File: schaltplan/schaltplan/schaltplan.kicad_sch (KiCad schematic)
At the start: 29 parts, among them SW1 Button 1, SW2 Button 2, SW3 Button 3, SW4 Button 4

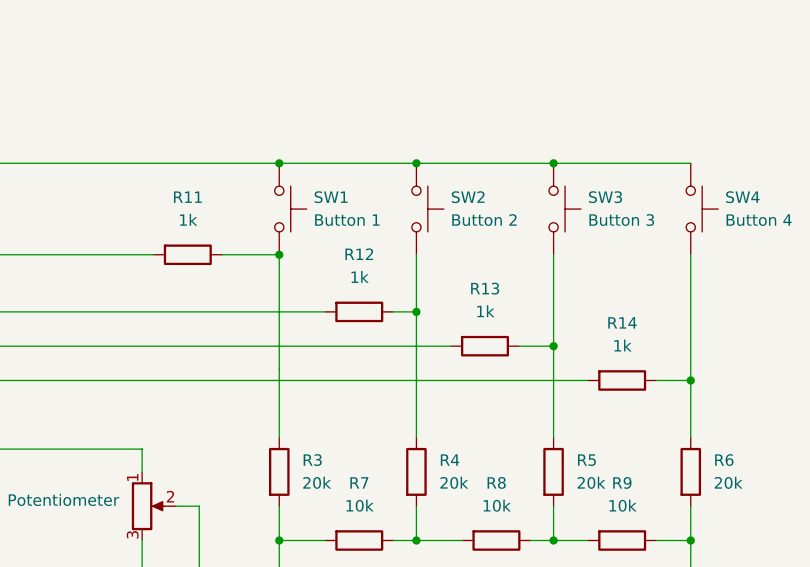
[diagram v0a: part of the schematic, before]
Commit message: schaltplan aktualisiert, hatte die falschen widerstandswerte eingetragen
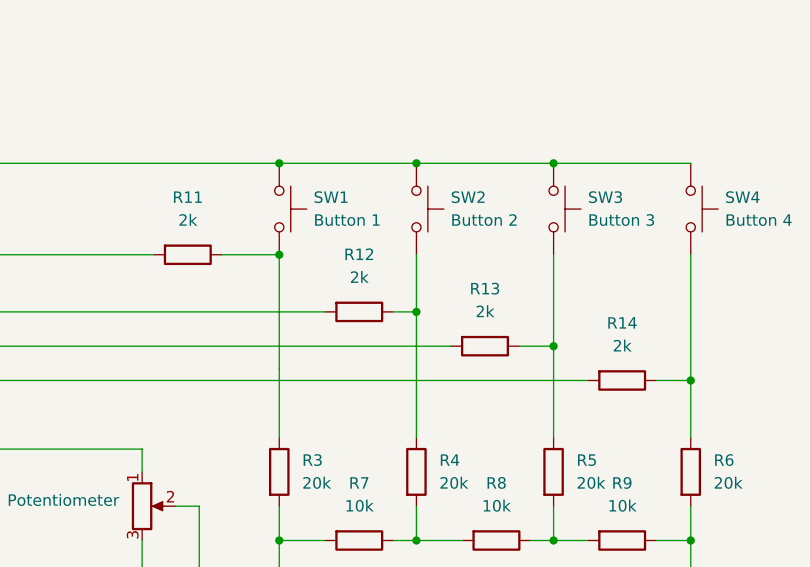
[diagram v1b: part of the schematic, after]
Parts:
- R11, R12, R13, R14: value 1k -> 2k
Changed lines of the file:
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@@
 			)
 		)
-		(property "Value" "1k"
+		(property "Value" "2k"
 			(at 162.56 85.09 90)
 			(effects
@@
 			)
 		)
-		(property "Value" "1k"
+		(property "Value" "2k"
 			(at 176.53 88.9 90)
 			(effects
@@
 			)
 		)
-		(property "Value" "1k"
+		(property "Value" "2k"
 			(at 143.51 78.74 90)
 			(effects
@@
 			)
 		)
-		(property "Value" "1k"
+		(property "Value" "2k"
 			(at 191.77 92.71 90)
 			(effects

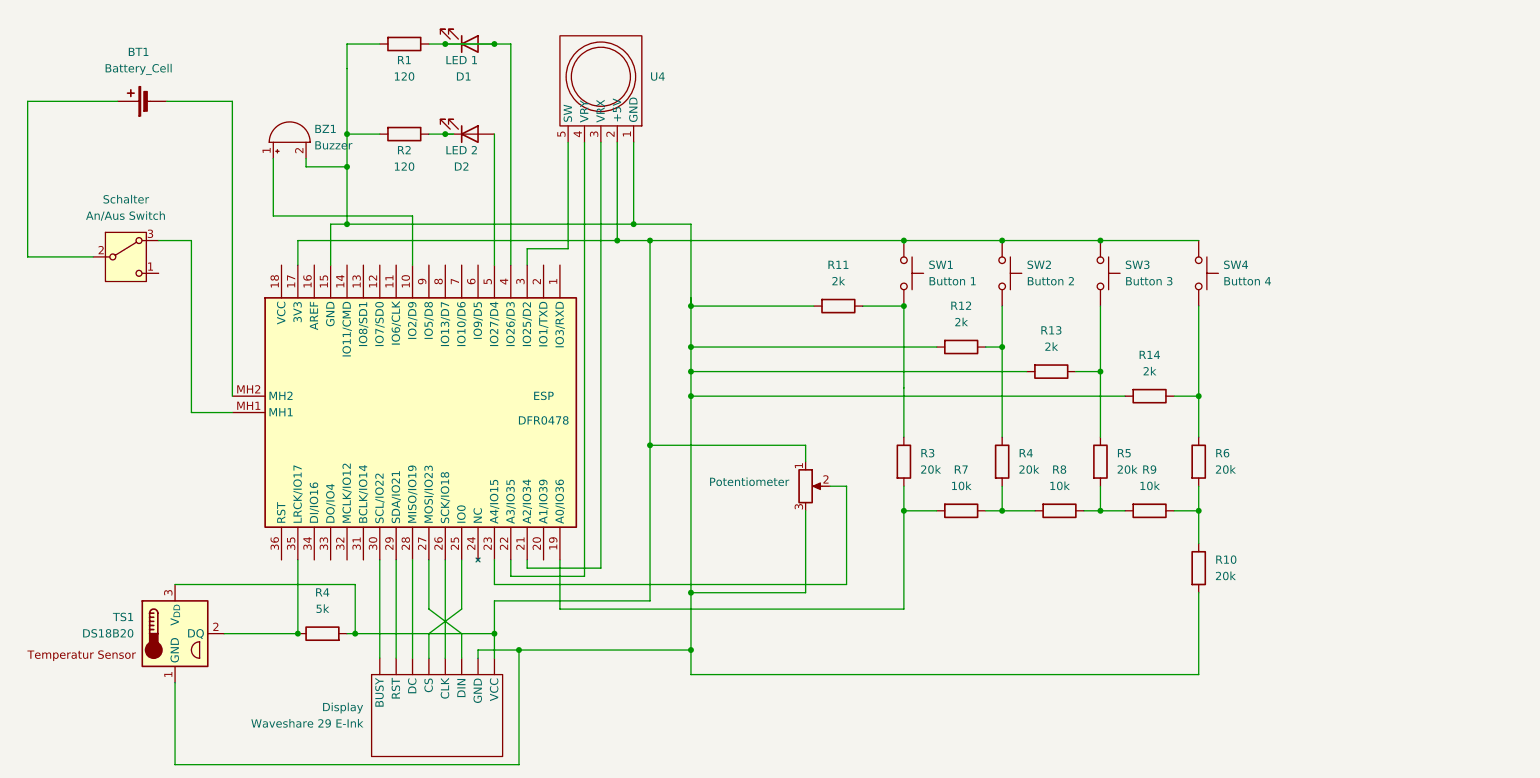
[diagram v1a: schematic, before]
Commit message: Add files via upload
Buzzer im Schaltplan angepasst
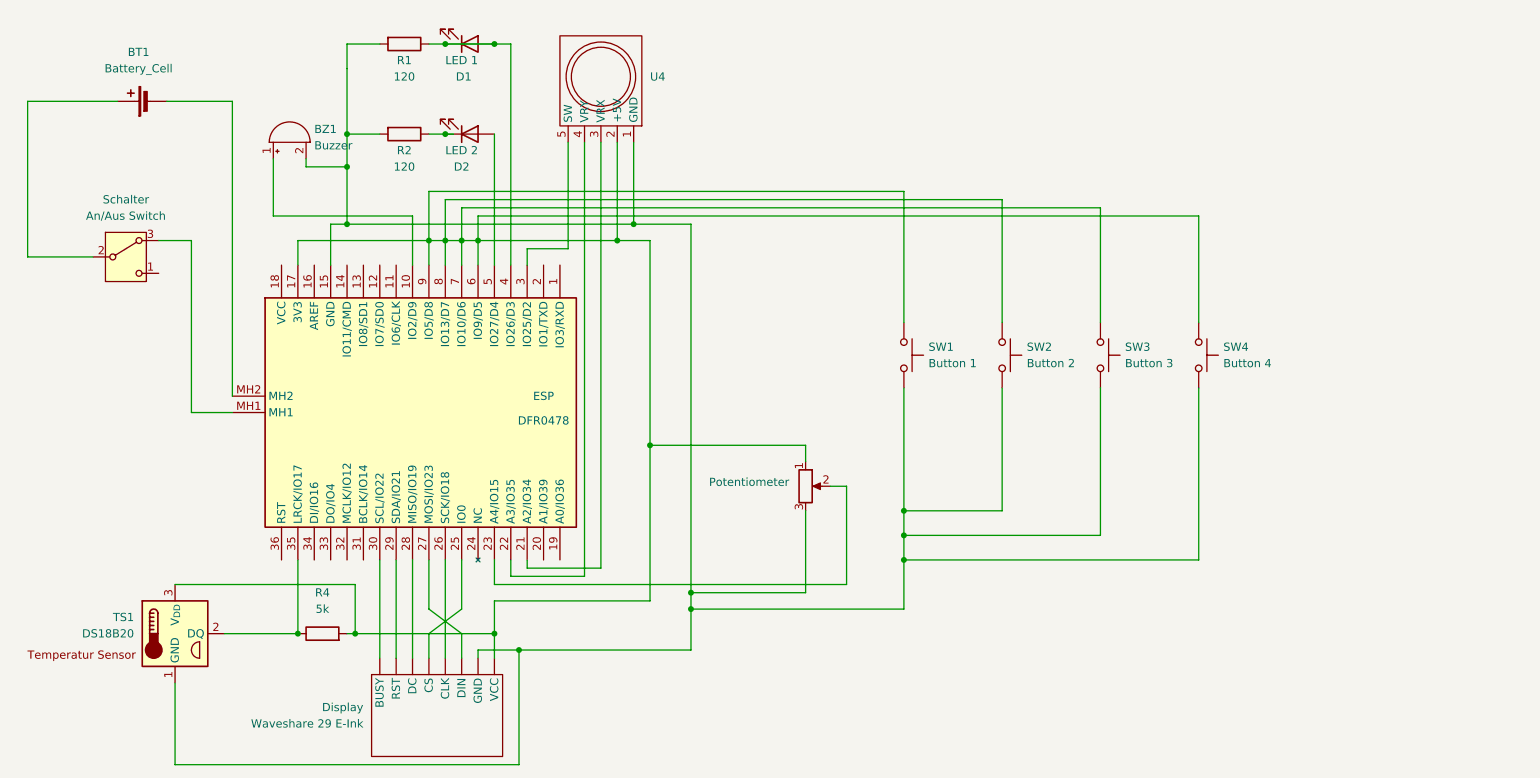
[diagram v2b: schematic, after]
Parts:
- removed R10, R3, R4, R5, R6: 20k, symbol Device:R
- removed R11, R12, R13, R14: 2k, symbol Device:R
- removed R7, R8, R9: 10k, symbol Device:R
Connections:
- net at BZ1.2 (-), Display. (VCC), ESP.15 (GND)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: now also SW1.2, SW2.2, SW3.2, SW4.2
- net at Display. (VCC), ESP.17 (3V3), Potentiometer.1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: now also ESP.6 (IO9/D5), ESP.7 (IO10/D6), ESP.8 (IO13/D7), ESP.9 (IO5/D8)
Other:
- moved on the sheet: SW1, SW2, SW3, SW4

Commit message: schaltplan korrigiert
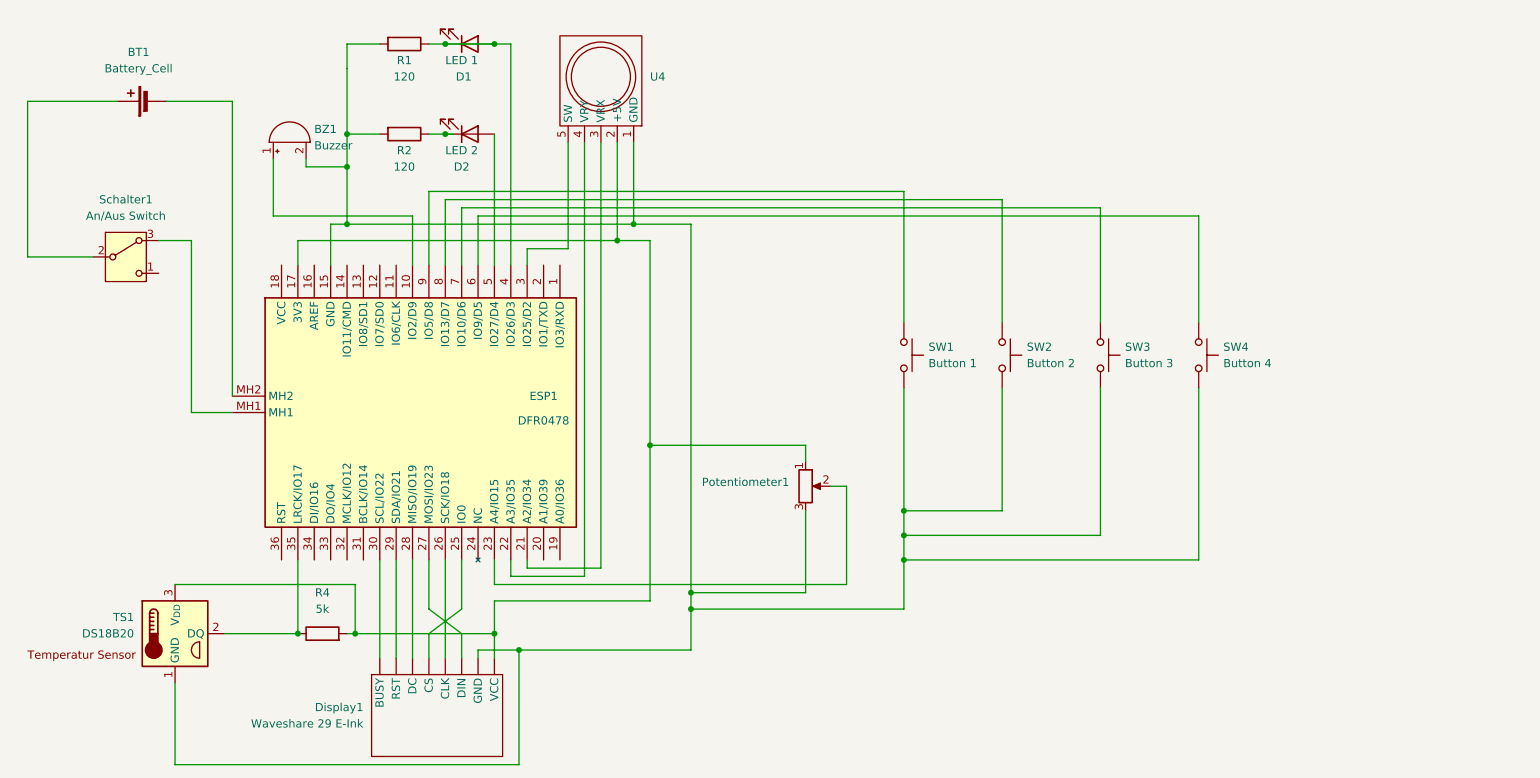
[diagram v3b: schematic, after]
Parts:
- renumbered Display to Display1, ESP to ESP1, Potentiometer to Potentiometer1, Schalter to Schalter1
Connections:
- new net: ESP1.7 (IO10/D6), SW3.1
- new net: ESP1.8 (IO13/D7), SW2.1
- new net: ESP1.9 (IO5/D8), SW1.1
- new net: Display1. (VCC), ESP1.17 (3V3), Potentiometer1.1, R4.2, TS1.3 (V_{DD}), U4.2 (+5V)
- new net: ESP1.6 (IO9/D5), SW4.1

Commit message: spannungsteiler zum schaltplan hinzugefügt und für messung an analog pin angeschlossen
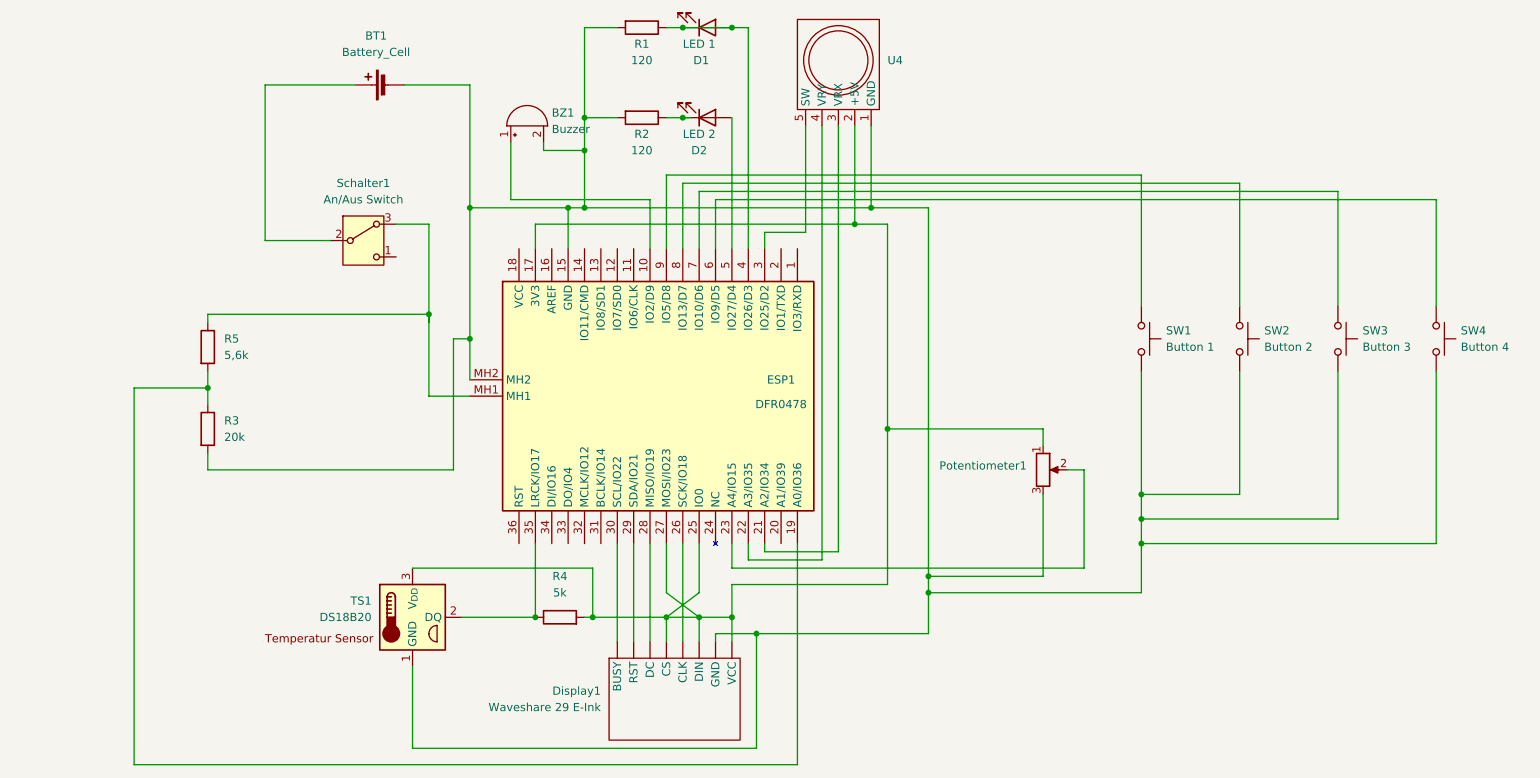
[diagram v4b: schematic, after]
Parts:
- added R3: 20k, symbol Device:R
- added R5: 5,6k, symbol Device:R
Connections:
- net at BZ1.2 (-), Display1. (VCC), ESP1.15 (GND)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: now also BT1.2 (-), ESP1.MH2, R3.2
- net at ESP1.MH1, Schalter1.3 (A): now also R5.1
- net at Display1. (VCC), ESP1.17 (3V3), Potentiometer1.1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: now also ESP1.25 (IO0), ESP1.27 (MOSI/IO23)
- net at Display1. (VCC): now also ESP1.30 (SCL/IO22); no longer ESP1.25 (IO0)
- net at ESP1.19 (A0/IO36): now also R3.1, R5.2
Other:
- moved on the sheet: BT1, BZ1, D1, D2, Display1, ESP1, Potentiometer1, R1, R2, R4, SW1, SW2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
